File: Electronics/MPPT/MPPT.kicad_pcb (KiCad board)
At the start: 2 copper layers, 172.7 x 116.8 mm, 151 parts, among them J1 Solar Array, J2 Battery, J3 Car Power, J4 CAN_In, J5 CAN_Out, Q1 NMOS, Q2 NMOS, SW1 RESET, SW2 CAN Address, U1 PQMC3-D12-S9-S, U2 Nucleo_L432KC, U3 UCC37321, U4 INA210, U5 ADM3055E, U6 INA210, U7 CDSOT23-T24CAN

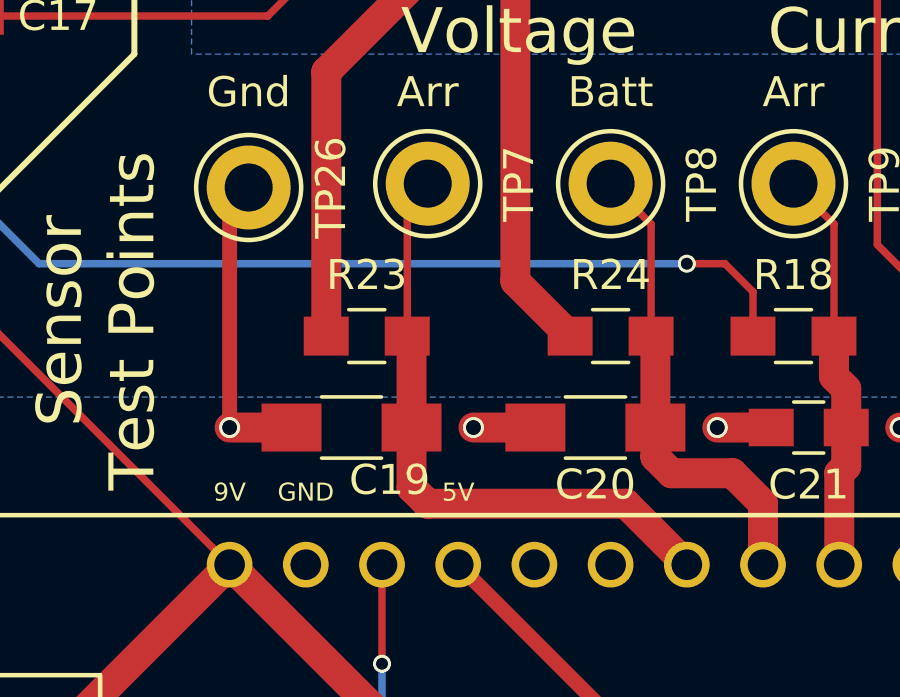
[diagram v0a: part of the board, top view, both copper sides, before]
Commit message: MPPT: Correct footprints on sensor filter capacitors
The voltage sensors' RC filter capacitors are now 0805 as they should be, rather than 1206 as they were before.
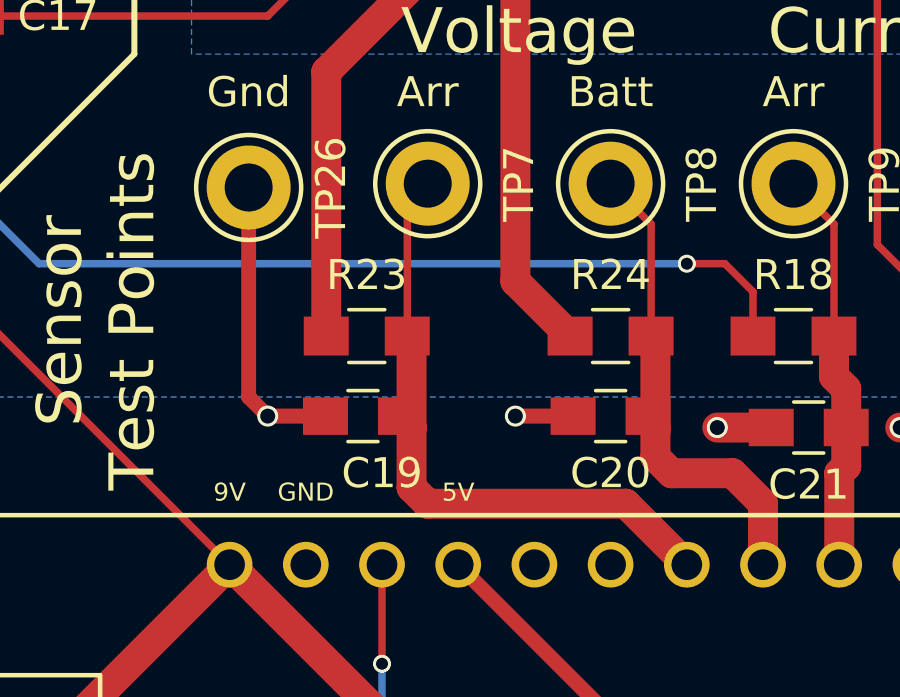
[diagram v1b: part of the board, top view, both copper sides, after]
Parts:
- C19, C20: footprint Capacitors_SMD:C_1206_HandSoldering -> Capacitors_SMD:C_0805_HandSoldering
- moved C20 0.63 mm to (87.6, 113.0)
- moved C19 0.54 mm to (79.4, 113.0)
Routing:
- net /Array_Voltage: track 20.7 -> 21.8 mm
- net /Battery_Voltage: track 16.0 -> 16.9 mm
- net GNDPWR: track 392.9 -> 392.2 mm

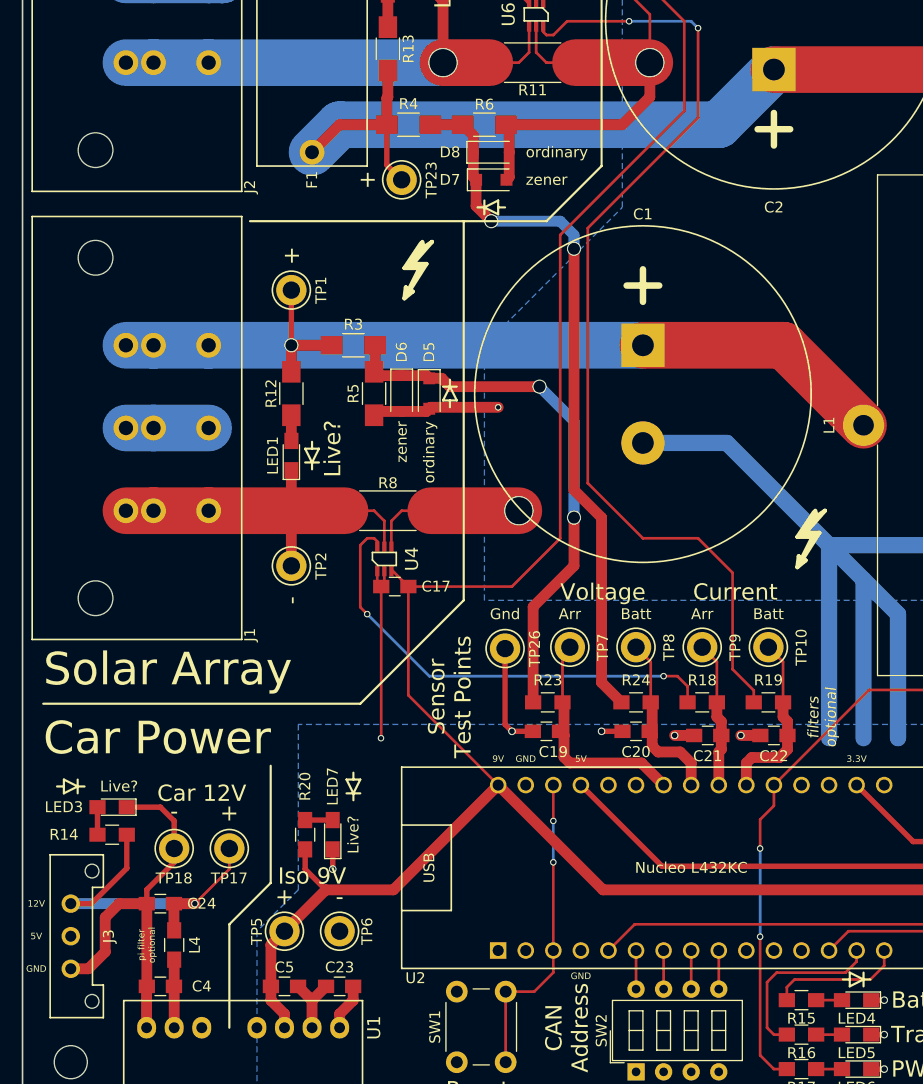
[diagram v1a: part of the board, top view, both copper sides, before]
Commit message: MPPT: Implement sensor and car power changes on PCB.
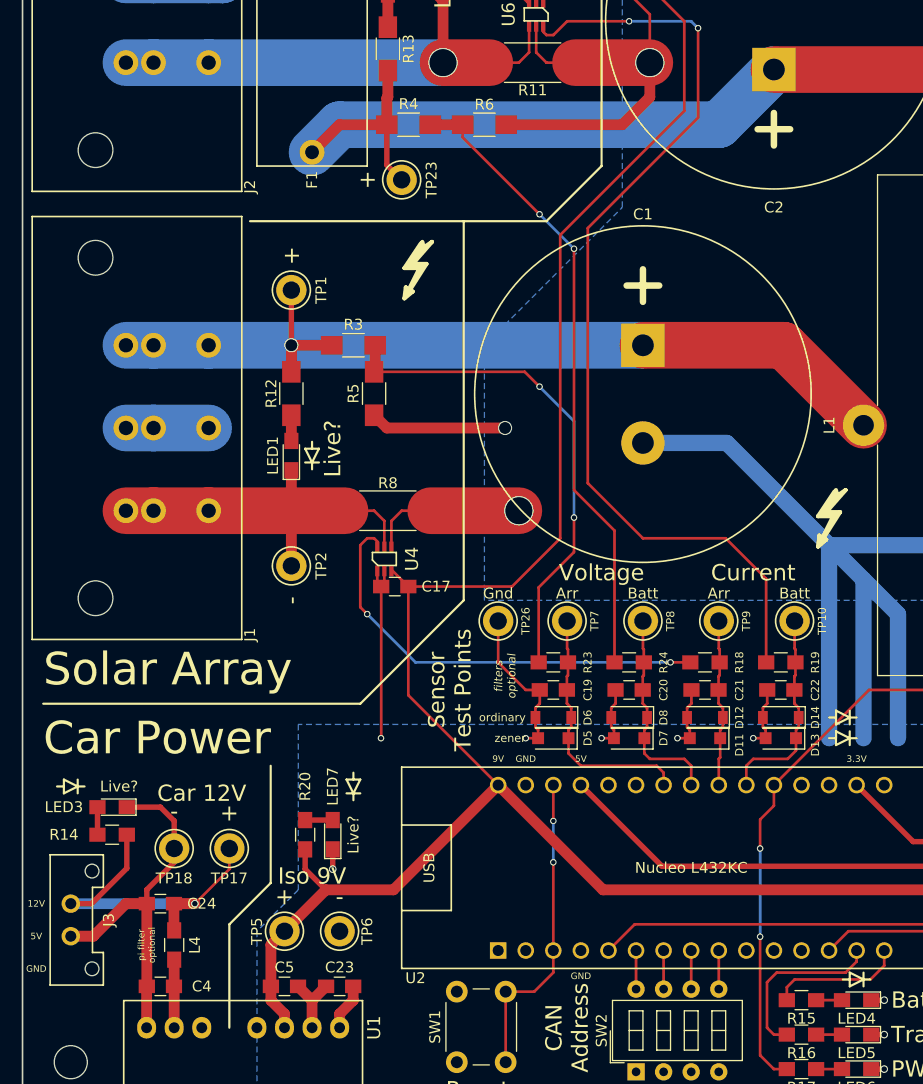
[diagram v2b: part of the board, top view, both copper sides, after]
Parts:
- added D11: 4V Zener, Diodes_SMD:D_SOD-123F, F.Cu at (94.0, 113.7)
- added D12: Diode, Diodes_SMD:D_SOD-123, F.Cu at (94.0, 111.8)
- added D13: 4V Zener, Diodes_SMD:D_SOD-123F, F.Cu at (101.0, 113.7)
- added D14: Diode, Diodes_SMD:D_SOD-123, F.Cu at (101.0, 111.8)
- D5, D7, D9: value Zener -> 4V Zener
- J3: footprint UTSVT_Connectors:Molex_MicroFit3.0_1x3xP3.00mm_PolarizingPeg_Vertical -> UTSVT_Connectors:Molex_MicroFit3.0_1x2xP3.00mm_PolarizingPeg_Vertical
- moved REF** 58.6 mm to (106.7, 113.7), turned to 270 degrees
- moved D8 53.6 mm to (87.0, 111.8), turned to 180 degrees
- moved D7 53.0 mm to (87.0, 113.7), turned to 180 degrees
- moved REF** 46.9 mm to (106.7, 111.8), turned to 270 degrees
- moved D5 33.7 mm to (80.0, 113.7), turned to 180 degrees
- moved D6 33.0 mm to (80.0, 111.8), turned to 180 degrees
- moved C22 4.24 mm to (101.0, 109.2)
- moved C21 4.20 mm to (94.0, 109.2)
- moved C19 3.86 mm to (80.0, 109.2)
- moved C20 3.86 mm to (87.0, 109.2)
- moved R19 3.86 mm to (101.0, 106.7)
- moved R24 3.74 mm to (87.0, 106.7)
- moved R23 3.72 mm to (80.0, 106.7)
- moved R18 3.69 mm to (94.0, 106.7)
- moved TP10 3.41 mm to (102.2, 102.9)
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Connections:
- D5 pad 1: Net-(D5-Pad1) -> /Array_Voltage
- D6 pad 1: Net-(D5-Pad1) -> /Array_Voltage
- D7 pad 1: Net-(D7-Pad1) -> /Battery_Voltage
- D8 pad 1: Net-(D7-Pad1) -> /Battery_Voltage
- J3 pad 2: Net-(J3-Pad2) -> GNDREF
- R23 pad 1: Net-(D5-Pad1) -> Net-(R23-Pad1)
- R24 pad 1: Net-(D7-Pad1) -> Net-(R24-Pad1)
- R3 pad 2: Net-(D5-Pad1) -> Net-(R23-Pad1)
- R4 pad 2: Net-(D7-Pad1) -> Net-(R24-Pad1)
- R5 pad 1: Net-(D5-Pad1) -> Net-(R23-Pad1)
- R6 pad 1: Net-(D7-Pad1) -> Net-(R24-Pad1)
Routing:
- net Net-(D7-Pad1): track 66.0 -> 0.00 mm, vias 2 -> 0
- net Net-(R24-Pad1): track 0.00 -> 58.3 mm, vias 0 -> 2
- net Net-(D5-Pad1): track 50.1 -> 0.00 mm, vias 2 -> 0
- net Net-(R23-Pad1): track 0.00 -> 46.2 mm, vias 0 -> 2
- net GNDPWR: track 392.2 -> 404.5 mm
- net GNDREF: track 36.3 -> 33.2 mm
- net /Battery_Current: track 16.5 -> 19.2 mm
- net /Battery_Voltage: track 16.9 -> 19.1 mm
- net Net-(R18-Pad1): track 42.8 -> 40.7 mm
- net /Array_Current: track 13.5 -> 15.5 mm
- net Net-(R19-Pad1): track 91.3 -> 89.6 mm
- net /Array_Voltage: track 21.8 -> 23.2 mm

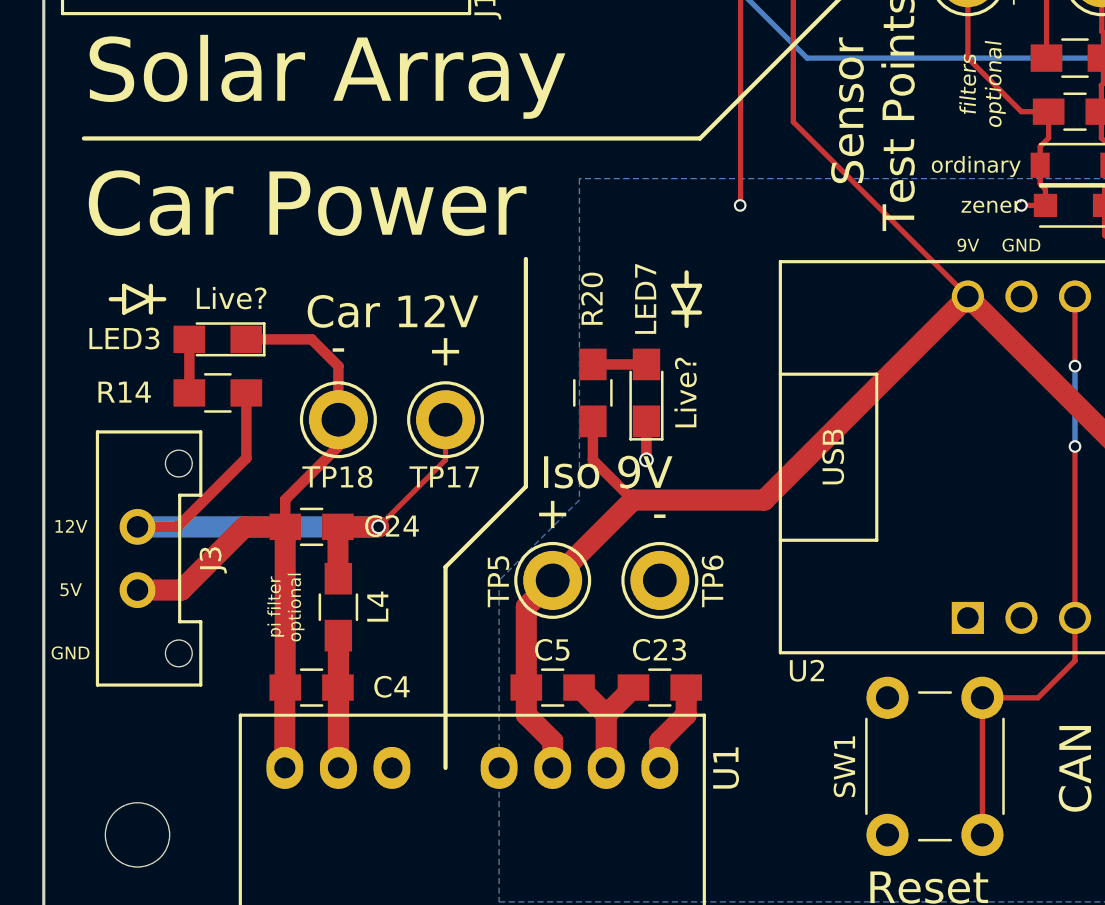
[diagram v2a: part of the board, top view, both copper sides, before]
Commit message: MPPT: Correct footprints for car power regulator capacitors
This involved rearranging much of the car power regulation block of the PCB, as the new footprints were rather large.
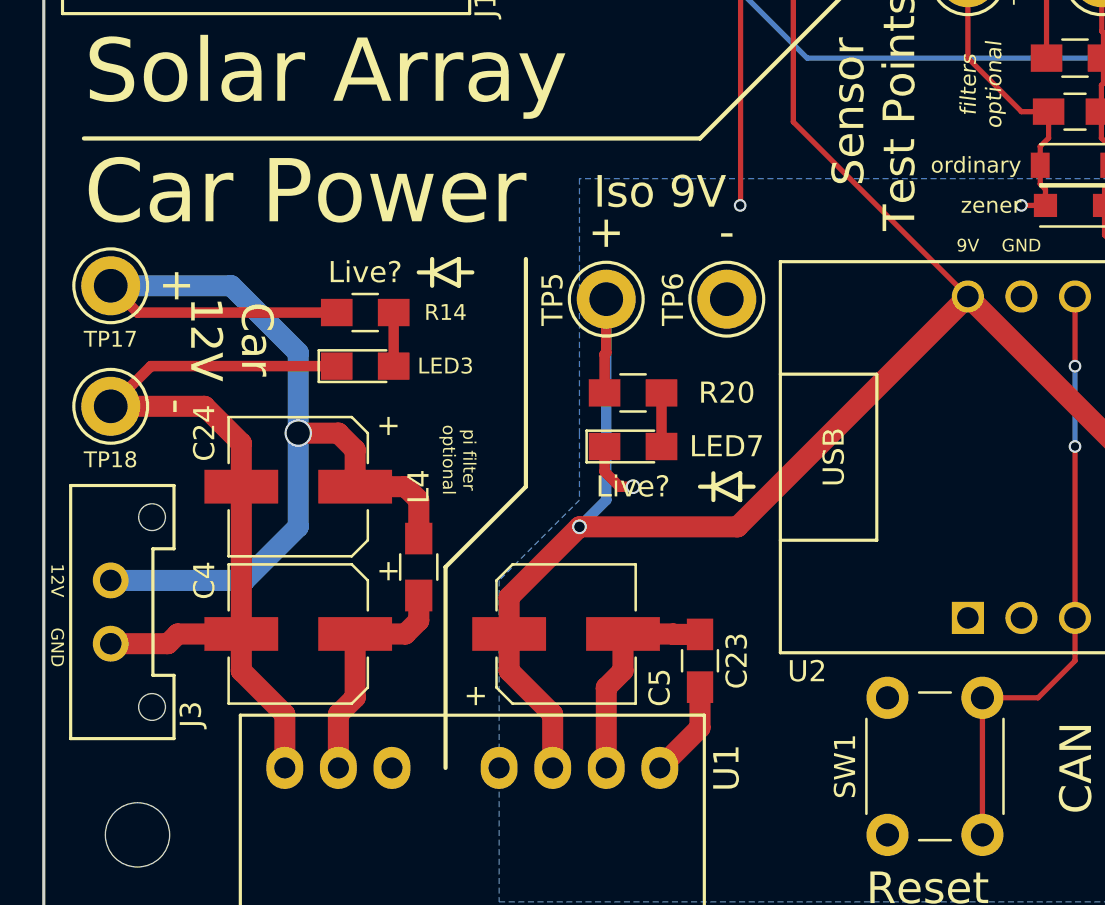
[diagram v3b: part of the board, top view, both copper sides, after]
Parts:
- C24, C5: footprint Capacitors_SMD:C_0805_HandSoldering -> Capacitors_SMD:CP_Elec_6.3x7.7
- C4: footprint Capacitors_SMD:C_0805_HandSoldering -> Capacitors_SMD:CP_Elec_6.3x5.3
- moved TP17 17.1 mm to (34.3, 117.5), turned to 270 degrees
- moved REF** 14.7 mm to (50.2, 116.8), turned to 90 degrees
- moved TP6 13.7 mm to (63.5, 118.1), turned to 0 degrees
- moved TP5 13.6 mm to (57.8, 118.1)
- moved TP18 10.8 mm to (34.3, 123.2), turned to 270 degrees
- moved REF** 9.09 mm to (63.5, 127.0), turned to 90 degrees
- moved R14 7.96 mm to (46.4, 118.7), turned to 180 degrees
- moved LED3 7.10 mm to (46.4, 121.3), turned to 0 degrees
- moved L4 4.26 mm to (48.9, 130.8)
- moved J3 2.84 mm to (34.3, 131.4)
- moved C5 2.62 mm to (55.9, 134.0)
- moved C4 2.62 mm to (43.2, 134.0)
- moved LED7 2.62 mm to (59.1, 125.1), turned to 0 degrees
- moved C23 2.29 mm to (62.2, 135.3), turned to 270 degrees
- moved C24 2.01 mm to (43.2, 127.0), turned to 180 degrees
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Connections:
- C24 pad 1: GNDREF -> +12V
- C24 pad 2: +12V -> GNDREF
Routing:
- net +12V: track 31.8 -> 49.5 mm
- net +9VA: track 306.4 -> 319.1 mm, vias 3 -> 4
- net GNDREF: track 33.2 -> 41.1 mm
- net GNDPWR: track 404.5 -> 409.7 mm
- net Net-(C4-Pad1): track 6.27 -> 11.1 mm

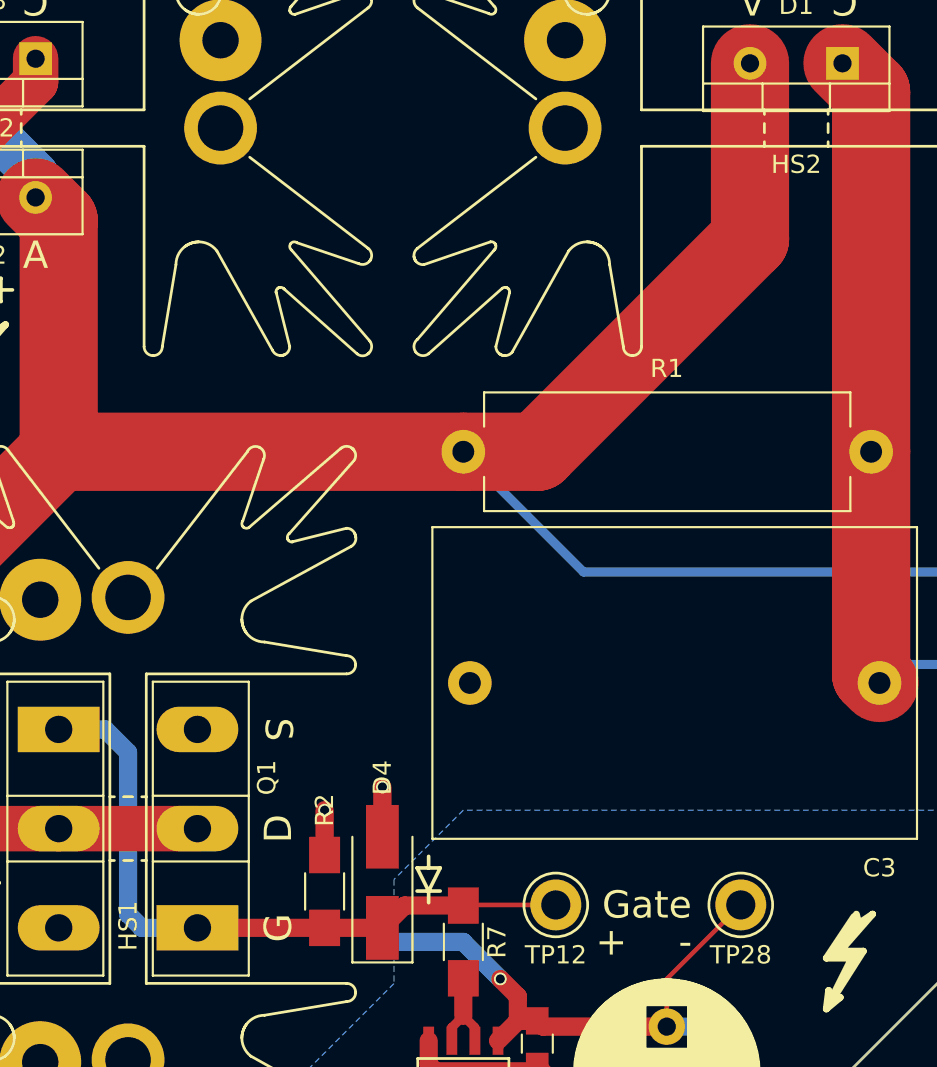
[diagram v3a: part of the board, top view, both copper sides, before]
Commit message: MPPT: Add extra labels to back side of PCB for MOSFETs and Schottkys.
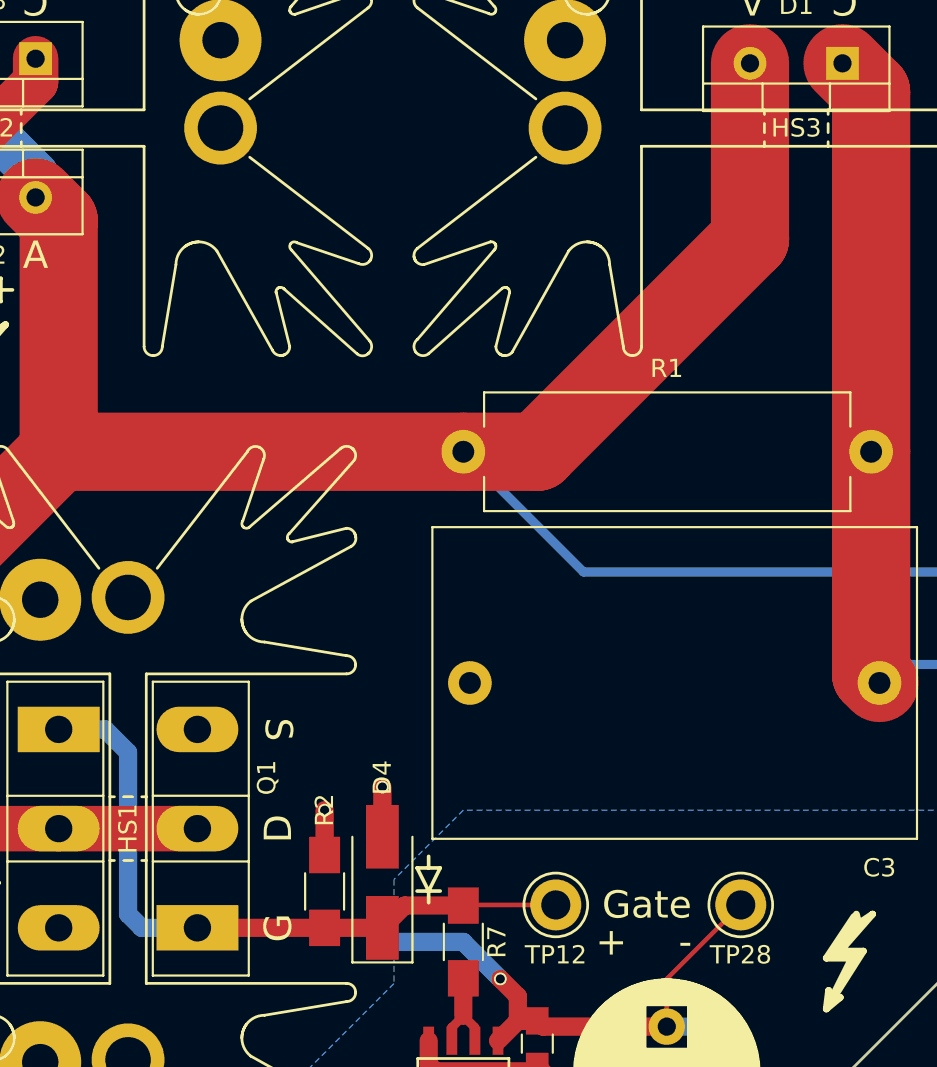
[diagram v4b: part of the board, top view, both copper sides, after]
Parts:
- renumbered HS2 to HS3
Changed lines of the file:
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@@
     (area 31.039999 31.039999 203.910001 148.030001)
     (thickness 1.6)
-    (drawings 139)
+    (drawings 151)
     (tracks 632)
     (zones 0)
@@
   (module Heatsinks:Heatsink_Fischer_SK129-STS_42x25mm_2xDrill2.5mm (layer F.Cu)
     (at 182.118 46.355 180)
-    (fp_text reference HS2 (at 0 -2 180) (layer F.SilkS)
+    (fp_text reference HS3 (at 0 0 180) (layer F.SilkS)
       (effects (font (size 1 1) (thickness 0.15)))
     )
@@
   (module Heatsinks:Heatsink_Fischer_SK129-STS_42x25mm_2xDrill2.5mm (layer F.Cu)
     (at 145.415 84.836 270)
-    (fp_text reference HS1 (at 5.334 0 270) (layer F.SilkS)
+    (fp_text reference HS1 (at 0 0 270) (layer F.SilkS)
       (effects (font (size 1 1) (thickness 0.15)))
     )
@@
     )
   )
+  (gr_text A (at 179.705 39.37) (layer B.SilkS)
+    (effects (font (size 1.5 1.5) (thickness 0.3)) (justify mirror))
+  )
+  (gr_text C (at 184.785 39.37) (layer B.SilkS)
+    (effects (font (size 1.5 1.5) (thickness 0.3)) (justify mirror))
+  )
+  (gr_text C (at 140.335 39.37) (layer B.SilkS)
+    (effects (font (size 1.5 1.5) (thickness 0.3)) (justify mirror))
+  )
+  (gr_text A (at 135.255 39.37) (layer B.SilkS)
+    (effects (font (size 1.5 1.5) (thickness 0.3)) (justify mirror))
+  )
+  (gr_text C (at 135.255 53.34) (layer B.SilkS)
+    (effects (font (size 1.5 1.5) (thickness 0.3)) (justify mirror))
+  )
+  (gr_text A (at 140.335 53.34) (layer B.SilkS)
+    (effects (font (size 1.5 1.5) (thickness 0.3)) (justify mirror))
+  )
+  (gr_text S (at 137.16 90.181 270) (layer B.SilkS)
+    (effects (font (size 1.5 1.5) (thickness 0.3)) (justify mirror))
+  )
+  (gr_text D (at 137.16 84.731 90) (layer B.SilkS)
+    (effects (font (size 1.5 1.5) (thickness 0.3)) (justify mirror))
+  )
+  (gr_text G (at 137.16 79.281 90) (layer B.SilkS)
+    (effects (font (size 1.5 1.5) (thickness 0.3)) (justify mirror))
+  )
+  (gr_text G (at 153.67 90.286 90) (layer B.SilkS)
+    (effects (font (size 1.5 1.5) (thickness 0.3)) (justify mirror))
+  )
+  (gr_text D (at 153.67 84.836 90) (layer B.SilkS)
+    (effects (font (size 1.5 1.5) (thickness 0.3)) (justify mirror))
+  )
+  (gr_text S (at 153.67 79.375 270) (layer B.SilkS)
+    (effects (font (size 1.5 1.5) (thickness 0.3)) (justify mirror))
+  )
   (gr_text ordinary (at 77.47 111.76) (layer F.SilkS)
     (effects (font (size 0.75 0.75) (thickness 0.15)) (justify right))
@@
     (effects (font (size 1.5 1.5) (thickness 0.3)))
   )
-  (gr_text "Optional: Ground Heat Sink\nbe careful about isolation!" (at 135.255 84.455 90) (layer B.SilkS)
+  (gr_text "Optional: Ground Heat Sink\nbe careful about isolation!" (at 134.62 84.455 90) (layer B.SilkS)
     (effects (font (size 1 1) (thickness 0.15)) (justify mirror))
   )
-  (gr_text "Optional: Ground Heat Sink\nbe careful about isolation!" (at 182.245 37.465) (layer B.SilkS)
+  (gr_text "Optional: Ground Heat Sink\nbe careful about isolation!" (at 182.245 36.83) (layer B.SilkS)
     (effects (font (size 1 1) (thickness 0.15)) (justify mirror))
   )
